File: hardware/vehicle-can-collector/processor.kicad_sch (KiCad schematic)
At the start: 9 parts, among them U201 ATSAMC21J18A-AUT, Y201 32.768kHz, Y202 12MHz

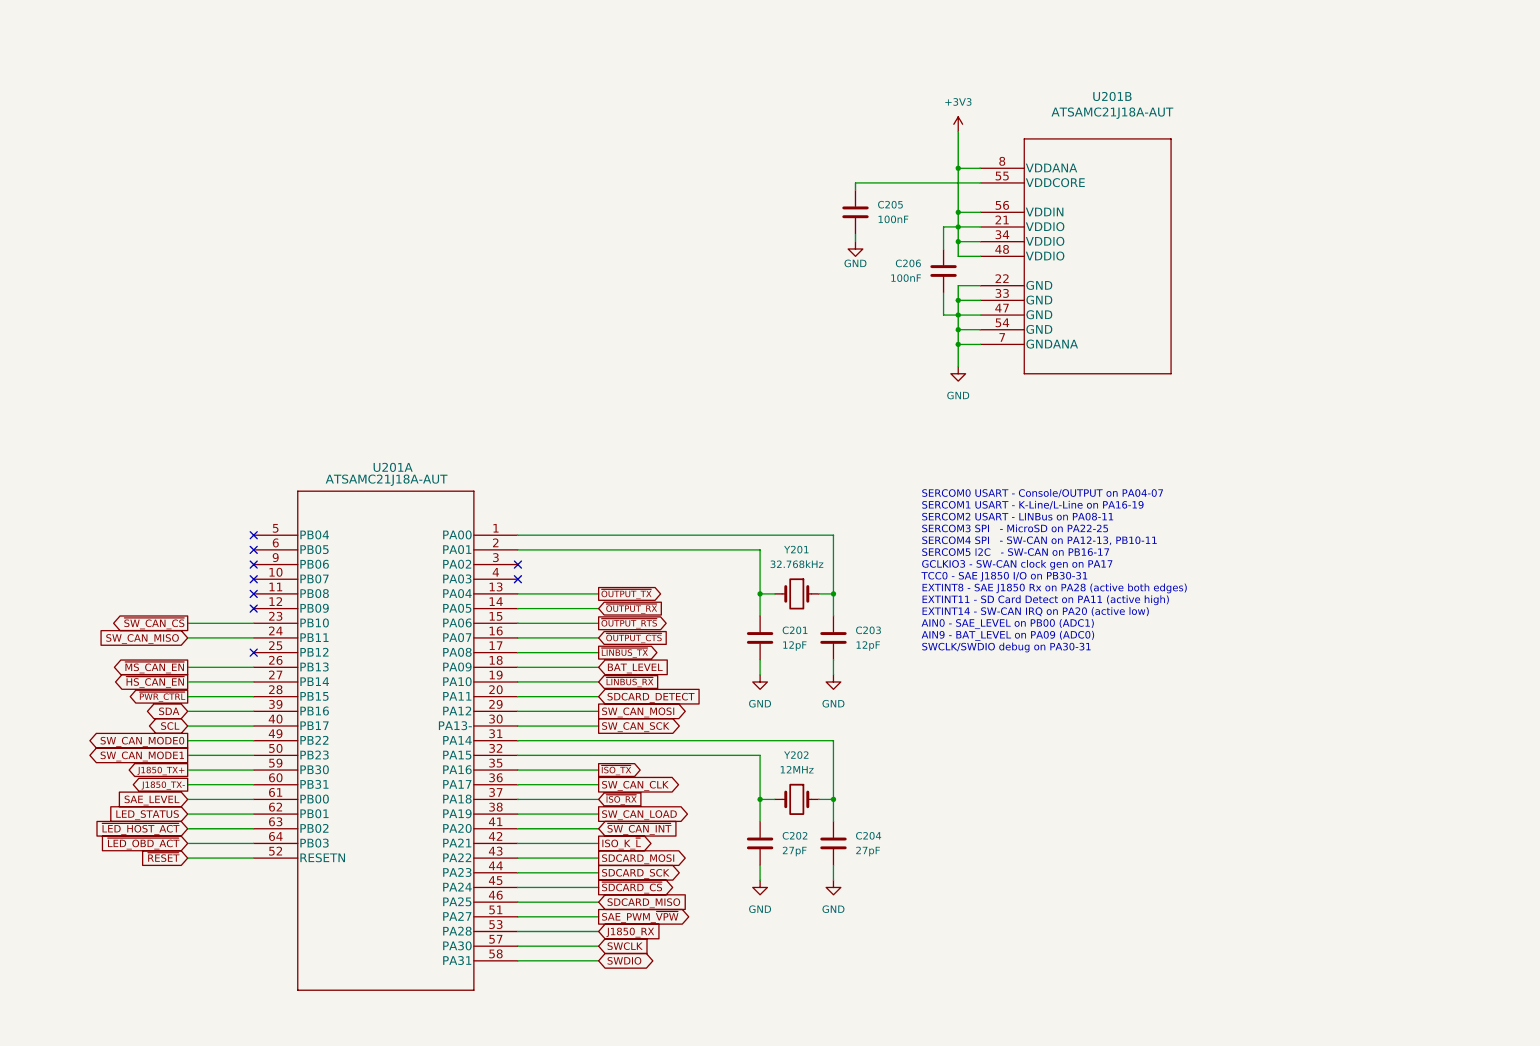
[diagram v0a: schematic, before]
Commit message: Added decoupling, more LEDs, update dts
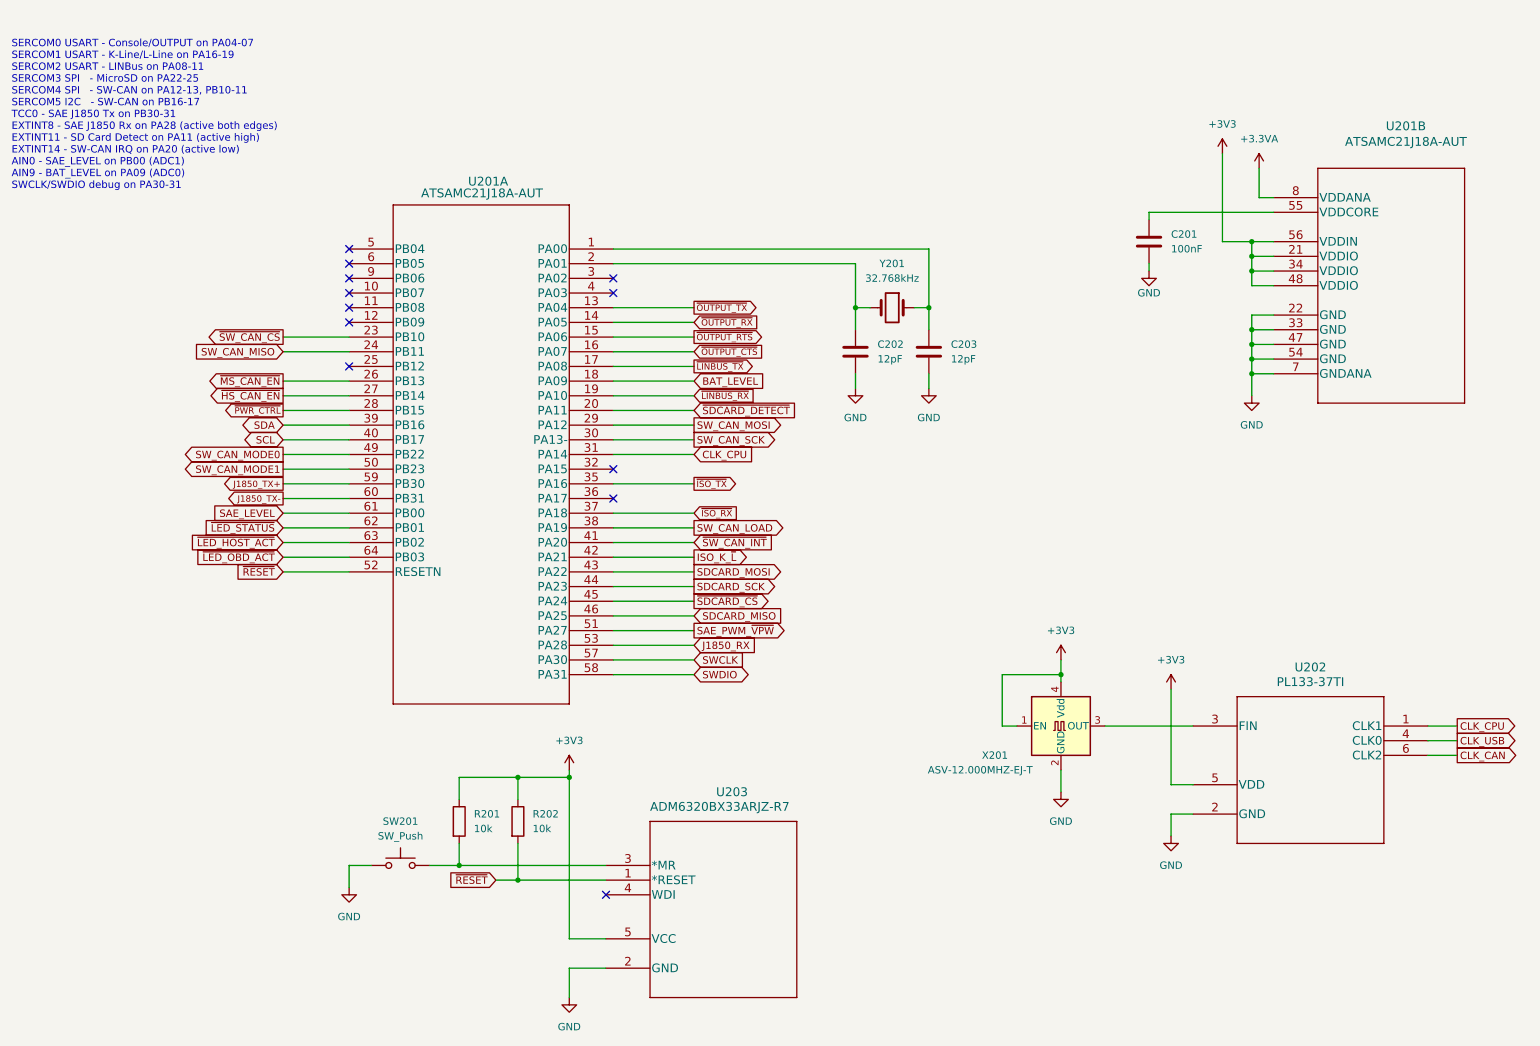
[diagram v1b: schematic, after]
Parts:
- removed C202, C204: 27pF, symbol Device:C
- removed C206: 100nF, symbol Device:C
- removed Y202: 12MHz, Crystal:Crystal_HC18-U_Horizontal, symbol Device:Crystal
- added R201, R202: 10k, symbol Device:R
- added SW201: SW_Push, symbol Switch:SW_Push
- added U202: PL133-37TI, SOT-23-6_MC_MCH, symbol UltraLibrarian:PL133-37TI
- added U203: ADM6320BX33ARJZ-R7, RJ_5_ADI, symbol UltraLibrarian:ADM6320BX33ARJZ-R7
- added X201: ASV-12.000MHZ-EJ-T, Oscillator:Oscillator_SMD_Abracon_ASV-4Pin_7.0x5.1mm, symbol Oscillator:ASV-xxxMHz
- renumbered C205 to C201, C201 to C202
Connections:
- net +3V3: now also R201.1, R202.1, U202.5 (VDD), U203.5 (VCC), X201.1 (EN), X201.4 (Vdd); no longer U201.8 (VDDANA)
- net GND: now also SW201.1, U202.2 (GND), U203.2 (GND), X201.2 (GND)
- net ~{RESET}: now also R202.2, U203.1 (*RESET)
- net CLK_CPU: now reaches U201.31 (PA14)
- net CLK_CPU: now also U202.1 (CLK1)
- net LED_STATUS renamed ~{LED_STATUS}
- net SDCARD_DETECT renamed ~{SDCARD_DETECT}
- net SW_CAN_CLK: no longer names the net of U201.36 (PA17)
- new net: R201.2, SW201.2, U203.3 (*MR)
- new net: U202.3 (FIN), X201.3 (OUT)
- new net +3.3VA: U201.8 (VDDANA)
- new net CLK_CAN: U202.6 (CLK2)
- new net CLK_USB: U202.4 (CLK0)
- no-connect marks 9 -> 12
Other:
- note added: "SERCOM0 USART - Console/OUTPUT on PA04-07 SERCOM1 USART - K-Line/L-Line on PA16-19 SERCOM2 USART - LINBus on PA08-11 SERCOM3 SPI - MicroSD on PA22-25 SERCOM4 SPI - SW-CAN on PA12-13, PB10-11 SERCOM5 I2C - SW-CAN on PB16-17 TCC0 - SAE J1850 Tx on PB30-31 EXTINT8 - SAE J1850 Rx on PA28 (active both edges) EXTINT11 - SD Card Detect on PA11 (active high) EXTINT14 - SW-CAN IRQ on PA20 (active low) AIN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"
- note removed: "SERCOM0 USART - Console/OUTPUT on PA04-07 SERCOM1 USART - K-Line/L-Line on PA16-19 SERCOM2 USART - LINBus on PA08-11 SERCOM3 SPI - MicroSD on PA22-25 SERCOM4 SPI - SW-CAN on PA12-13, PB10-11 SERCOM5 I2C - SW-CAN on PB16-17 GCLKIO3 - SW-CAN clock gen on PA17 TCC0 - SAE J1850 I/O on PB30-31 EXTINT8 - SAE J1850 Rx on PA28 (active both edges) EXTINT11 - SD Card Detect on PA11 (active high) EXTINT14 -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"
- company: (none) -> Gavin Hurlbut
- title: (none) -> Vehicle CAN Collector
- moved on the sheet: C201, C202, C203, U201A, U201B, Y201
